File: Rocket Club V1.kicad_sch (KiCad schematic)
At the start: 8 parts, among them IC1 STM32H573RIT6, J1 USB4135-GF-A_REVA, U1 H3LIS100DLTR, U2 LSM6DSOTR, U3 MAX-M8W-0, U4 MT25TL01GBBB8ESF-0AAT, U5 STLINK-V3MODS

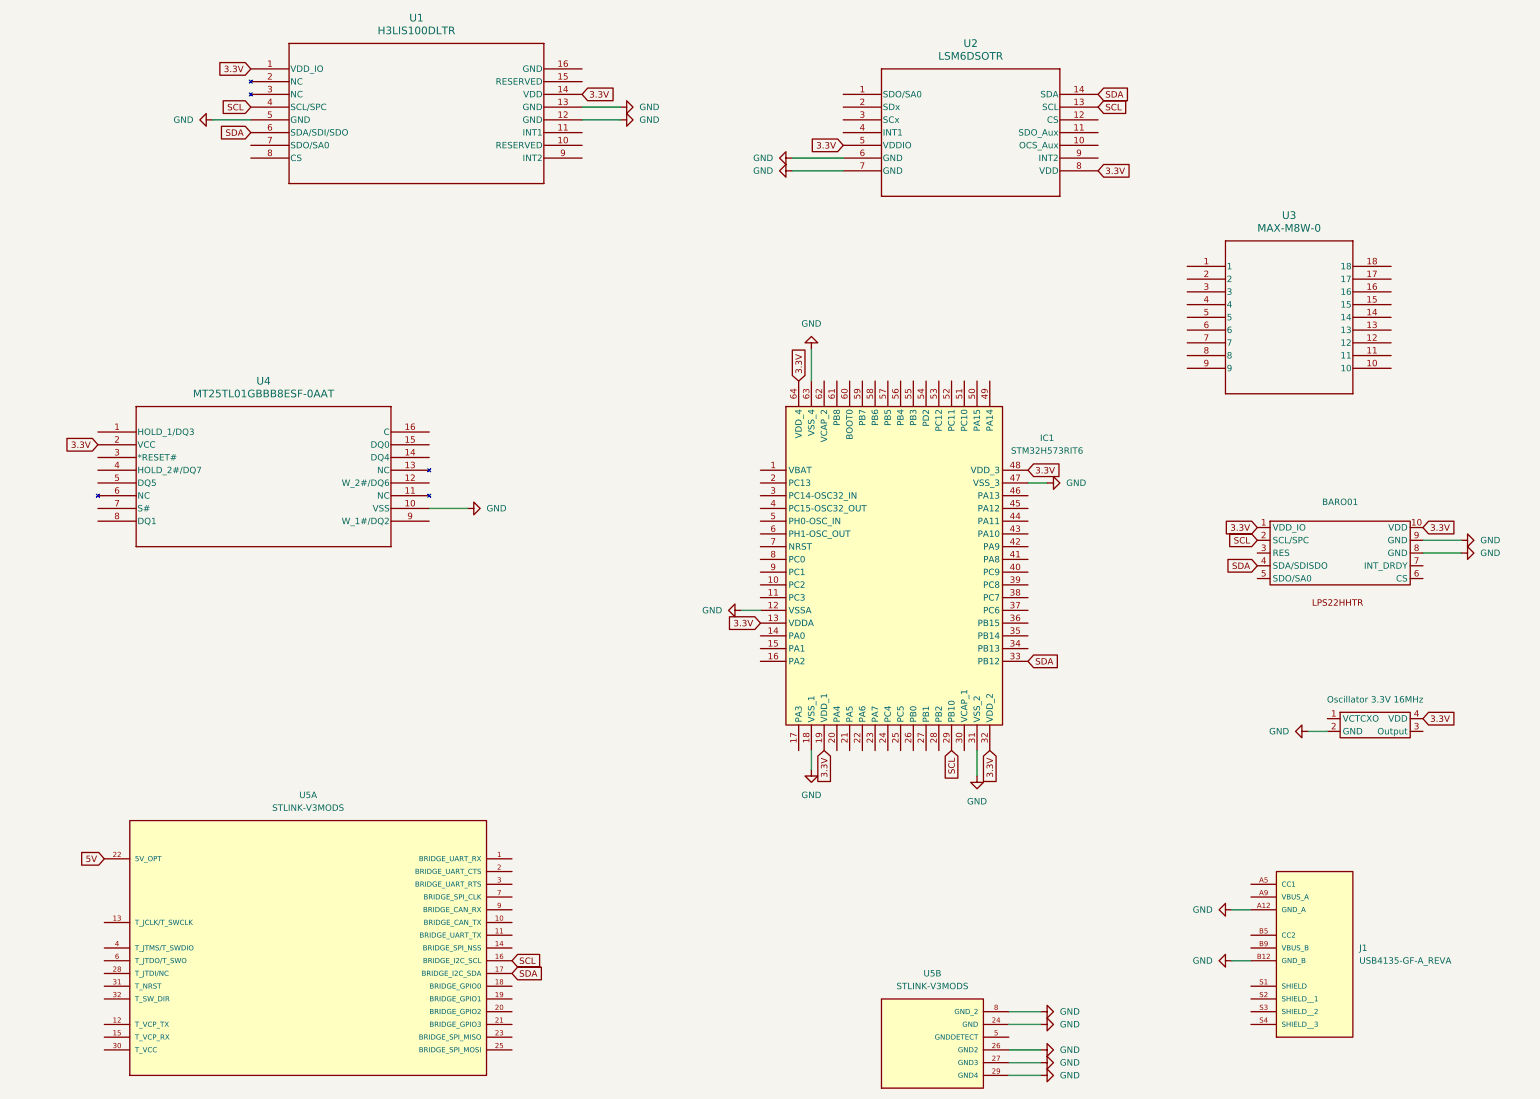
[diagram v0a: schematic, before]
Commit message: LSM fully wired
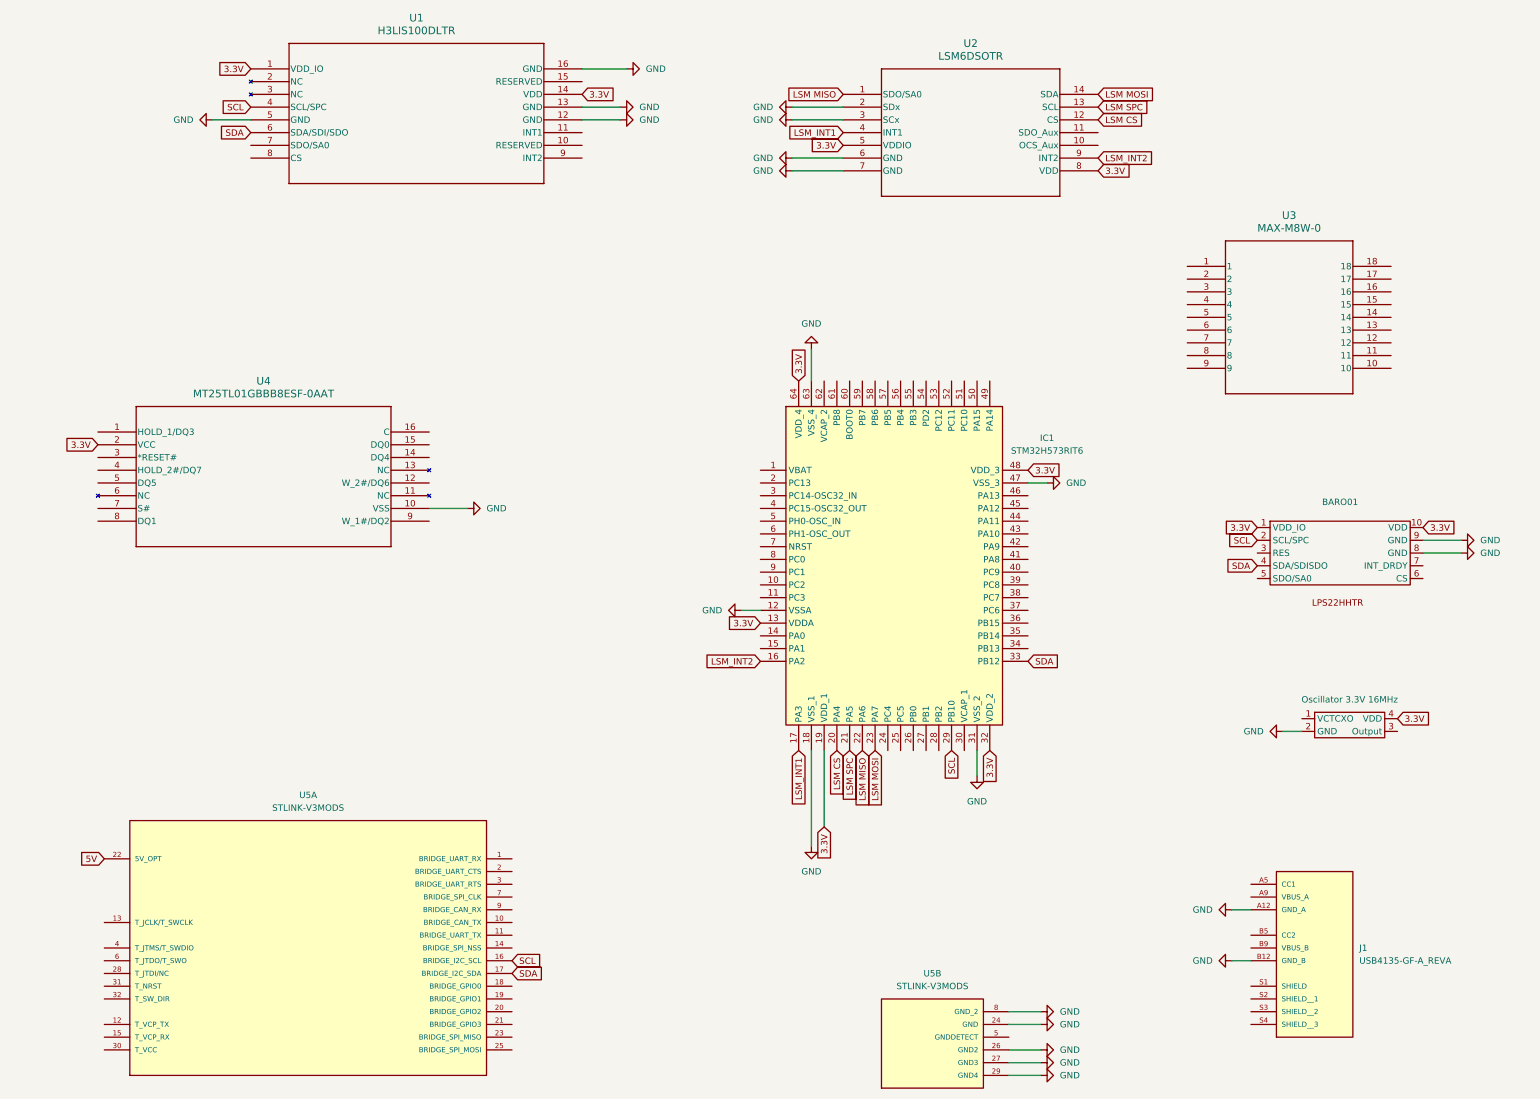
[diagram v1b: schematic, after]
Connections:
- net GND: now also U1.16 (GND), U2.2 (SDx), U2.3 (SCx)
- net SCL: no longer U2.13 (SCL)
- net SDA: no longer U2.14 (SDA)
- net LSM MISO: now reaches U2.1 (SDO/SA0)
- net LSM MISO: now also IC1.22 (PA6)
- net LSM CS: now reaches U2.12 (CS)
- net LSM CS: now also IC1.20 (PA4)
- net LSM_INT1: now reaches U2.4 (INT1)
- net LSM_INT1: now also IC1.17 (PA3)
- net LSM_INT2: now reaches U2.9 (INT2)
- net LSM_INT2: now also IC1.16 (PA2)
- net LSM SPC: now reaches IC1.21 (PA5)
- net LSM SPC: now also U2.13 (SCL)
- net LSM MOSI: now reaches IC1.23 (PA7)
- net LSM MOSI: now also U2.14 (SDA)

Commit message: Both IMU's, BARO, and NOR(?) Completed
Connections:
- net LSM MISO is gone; now on net MISO: IC1.22 (PA6), U2.1 (SDO/SA0)
- net LSM MOSI is gone; now on net MOSI: IC1.23 (PA7), U2.14 (SDA)
- net LSM SPC is gone; now on net SCK: IC1.21 (PA5), U2.13 (SCL)
- net LSM CS: now also IC1.27 (PB1); no longer IC1.20 (PA4)
- net LSM_INT1: now also IC1.14 (PA0); no longer IC1.17 (PA3)
- net LSM_INT2: now also IC1.15 (PA1); no longer IC1.16 (PA2)
- net H3_INT1: now reaches U1.11 (INT1)
- net H3_INT1: now also IC1.16 (PA2)
- net MISO: now reaches U1.7 (SDO/SA0)
- net MISO: now also U4.8 (DQ1)
- net H3 CS: now reaches U1.8 (CS)
- net H3 CS: now also IC1.28 (PB2)
- net H3_INT2: now reaches U1.9 (INT2)
- net H3_INT2: now also IC1.17 (PA3)
- net MT25 I/O 4: now reaches IC1.10 (PC2)
- net MT25 I/O 4: now also U4.14 (DQ4)
- net MT25 I/O 5: now reaches IC1.11 (PC3)
- net MT25 I/O 5: now also U4.5 (DQ5)
- net LPS CS: now reaches IC1.26 (PB0)
- net MT25 I/O 6/Protect 2: now reaches IC1.37 (PC6)
- net MT25 I/O 6/Protect 2: now also U4.12 (W_2#/DQ6)
- net MT25 I/O 7/Hold 2: now reaches IC1.38 (PC7)
- net MT25 I/O 7/Hold 2: now also U4.4 (HOLD_2#/DQ7)
- net MT25 CS: now reaches IC1.55 (PB3)
- net MT25 CS: now also U4.7 (S#)
- net MT25 I/O 2/Protect 1: now reaches IC1.8 (PC0)
- net MT25 I/O 2/Protect 1: now also U4.9 (W_1#/DQ2)
- net MT25 I/O 3/Hold: now reaches IC1.9 (PC1)
- net MT25 I/O 3/Hold: now also U4.1 (HOLD_1/DQ3)
- net MOSI: now reaches U4.15 (DQ0)
- net MOSI: now also U1.6 (SDA/SDI/SDO)
- net SCK: now reaches U4.16 (C)
- net SCK: now also U1.4 (SCL/SPC)
- net MT25 RESET: now reaches U4.3 (*RESET#)
- removed net SCL: IC1.29 (PB10), U1.4 (SCL/SPC), U5.16 (BRIDGE_I2C_SCL)
- removed net SDA: IC1.33 (PB12), U1.6 (SDA/SDI/SDO), U5.17 (BRIDGE_I2C_SDA)
- new net LPS_INT1: IC1.20 (PA4)
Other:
- moved on the sheet: U3, U4
